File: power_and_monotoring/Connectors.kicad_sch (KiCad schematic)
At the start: 4 parts, among them J2 HLE-108-02-L-DV-BE-K-TR, J3 HLE-108-02-L-DV-BE-K-TR, J4 HLE-108-02-L-DV-BE-K-TR, J5 HLE-108-02-L-DV-BE-K-TR

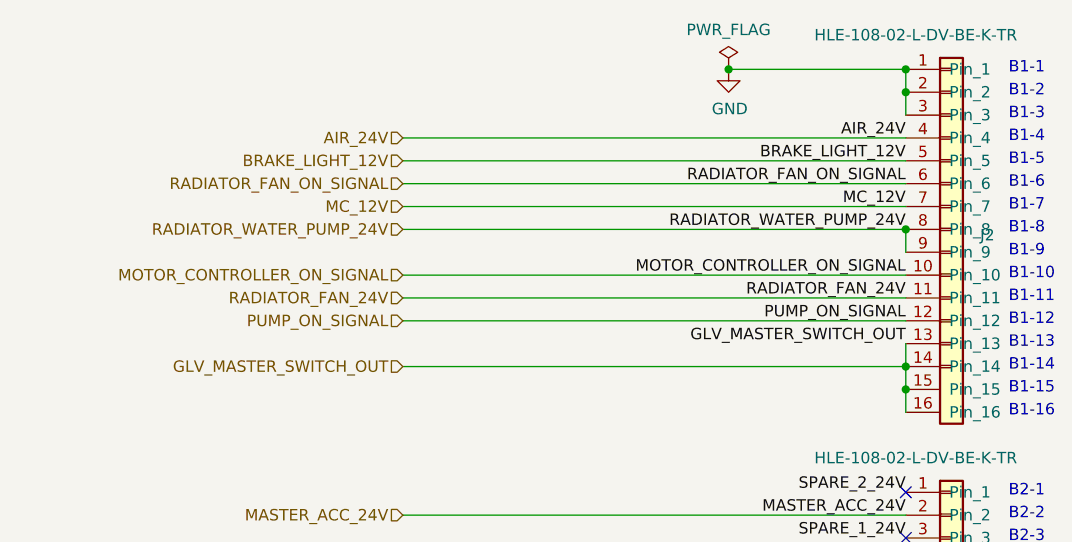
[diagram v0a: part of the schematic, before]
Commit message: first connections done (not perfect yet)
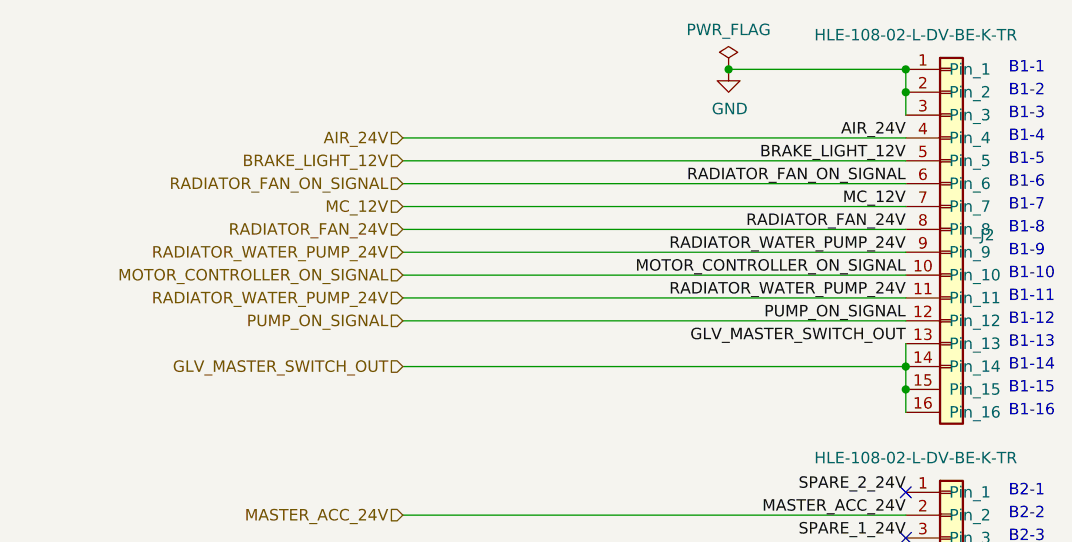
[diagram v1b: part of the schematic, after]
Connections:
- net RADIATOR_FAN_24V: now also J2.8 (Pin_8); no longer J2.11 (Pin_11)
- net RADIATOR_WATER_PUMP_24V: now also J2.11 (Pin_11); no longer J2.8 (Pin_8)
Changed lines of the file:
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@@
   (junction (at 193.675 96.52) (diameter 0) (color 0 0 0 0)
-  )
-  (junction (at 193.675 81.28) (diameter 0) (color 0 0 0 0)
   )
   (junction (at 193.675 63.5) (diameter 0) (color 0 0 0 0)
@@
     (stroke (width 0) (type default))
   )
-  (wire (pts (xy 193.675 81.28) (xy 193.675 83.82))
-    (stroke (width 0) (type default))
-  )
   (wire (pts (xy 137.795 128.27) (xy 193.675 128.27))
     (stroke (width 0) (type default))
   )
+  (wire (pts (xy 137.795 83.82) (xy 193.675 83.82))
+    (stroke (width 0) (type default))
+  )
   (wire (pts (xy 173.99 63.5) (xy 193.675 63.5))
     (stroke (width 0) (type default))
@@
     (stroke (width 0) (type default))
   )
+  (wire (pts (xy 137.795 81.28) (xy 193.675 81.28))
+    (stroke (width 0) (type default))
+  )
   (wire (pts (xy 137.795 73.66) (xy 193.675 73.66))
     (stroke (width 0) (type default))
@@
     (stroke (width 0) (type default))
   )
+  (wire (pts (xy 137.795 140.97) (xy 193.675 140.97))
+    (stroke (width 0) (type default))
+  )
+  (wire (pts (xy 137.795 118.11) (xy 193.675 118.11))
+    (stroke (width 0) (type default))
+  )
   (wire (pts (xy 137.795 88.9) (xy 193.675 88.9))
     (stroke (width 0) (type default))
   )
-  (wire (pts (xy 137.795 140.97) (xy 193.675 140.97))
-    (stroke (width 0) (type default))
-  )
-  (wire (pts (xy 137.795 118.11) (xy 193.675 118.11))
-    (stroke (width 0) (type default))
-  )
   (wire (pts (xy 137.795 86.36) (xy 193.675 86.36))
     (stroke (width 0) (type default))
@@
     (stroke (width 0) (type default))
   )
-  (wire (pts (xy 137.795 81.28) (xy 193.675 81.28))
-    (stroke (width 0) (type default))
-  )
   (wire (pts (xy 137.795 91.44) (xy 193.675 91.44))
     (stroke (width 0) (type default))
@@
     (effects (font (size 1.27 1.27)) (justify right bottom))
   )
+  (label "RADIATOR_WATER_PUMP_24V" (at 193.675 88.9 180) (fields_autoplaced)
+    (effects (font (size 1.27 1.27)) (justify right bottom))
+  )
   (label "MC_OK_INDICATOR" (at 193.675 211.455 180) (fields_autoplaced)
     (effects (font (size 1.27 1.27)) (justify right bottom))
@@
     (effects (font (size 1.27 1.27)) (justify right bottom))
   )
-  (label "RADIATOR_FAN_24V" (at 193.675 88.9 180) (fields_autoplaced)
-    (effects (font (size 1.27 1.27)) (justify right bottom))
-  )
   (label "GLV_MASTER_SWITCH_OUT" (at 193.675 93.98 180) (fields_autoplaced)
     (effects (font (size 1.27 1.27)) (justify right bottom))
@@
     (effects (font (size 1.27 1.27)) (justify right bottom))
   )
+  (label "RADIATOR_WATER_PUMP_24V" (at 193.675 83.82 180) (fields_autoplaced)
+    (effects (font (size 1.27 1.27)) (justify right bottom))
+  )
   (label "MC_12V" (at 193.675 78.74 180) (fields_autoplaced)
     (effects (font (size 1.27 1.27)) (justify right bottom))
@@
     (effects (font (size 1.27 1.27)) (justify right bottom))
   )
-  (label "RADIATOR_WATER_PUMP_24V" (at 193.675 81.28 180) (fields_autoplaced)
-    (effects (font (size 1.27 1.27)) (justify right bottom))
-  )
   (label "SHOULDER_RESET" (at 193.675 184.15 180) (fields_autoplaced)
     (effects (font (size 1.27 1.27)) (justify right bottom))
@@
     (effects (font (size 1.27 1.27)) (justify right bottom))
   )
+  (label "RADIATOR_FAN_24V" (at 193.675 81.28 180) (fields_autoplaced)
+    (effects (font (size 1.27 1.27)) (justify right bottom))
+  )
   (label "DASH_BSPD_LED" (at 193.675 168.91 180) (fields_autoplaced)
     (effects (font (size 1.27 1.27)) (justify right bottom))
@@
     (effects (font (size 1.27 1.27)) (justify right bottom))
   )
+  (hierarchical_label "RADIATOR_WATER_PUMP_24V" (shape input) (at 137.795 83.82 180) (fields_autoplaced)
+    (effects (font (size 1.27 1.27)) (justify right))
+  )
   (hierarchical_label "PRESSURE{slash}TEMP_SENSOR_3_5V" (shape input) (at 137.795 161.29 180) (fields_autoplaced)
     (effects (font (size 1.27 1.27)) (justify right))
@@
     (effects (font (size 1.27 1.27)) (justify right))
   )
+  (hierarchical_label "RADIATOR_FAN_24V" (shape input) (at 137.795 81.28 180) (fields_autoplaced)
+    (effects (font (size 1.27 1.27)) (justify right))
+  )
+  (hierarchical_label "RADIATOR_WATER_PUMP_24V" (shape input) (at 137.795 88.9 180) (fields_autoplaced)
+    (effects (font (size 1.27 1.27)) (justify right))
+  )
   (hierarchical_label "DATALOGGER_24V" (shape input) (at 137.795 135.89 180) (fields_autoplaced)
     (effects (font (size 1.27 1.27)) (justify right))
@@
     (effects (font (size 1.27 1.27)) (justify right))
   )
-  (hierarchical_label "RADIATOR_FAN_24V" (shape input) (at 137.795 88.9 180) (fields_autoplaced)
-    (effects (font (size 1.27 1.27)) (justify right))
-  )
   (hierarchical_label "POWER_SIGNAL" (shape input) (at 137.795 181.61 180) (fields_autoplaced)
     (effects (font (size 1.27 1.27)) (justify right))
@@
     (effects (font (size 1.27 1.27)) (justify right))
   )
-  (hierarchical_label "RADIATOR_WATER_PUMP_24V" (shape input) (at 137.795 81.28 180) (fields_autoplaced)
-    (effects (font (size 1.27 1.27)) (justify right))
-  )

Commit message: Final
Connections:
- no-connect marks 26 -> 28
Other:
- moved on the sheet: J2, J3, J4, J5

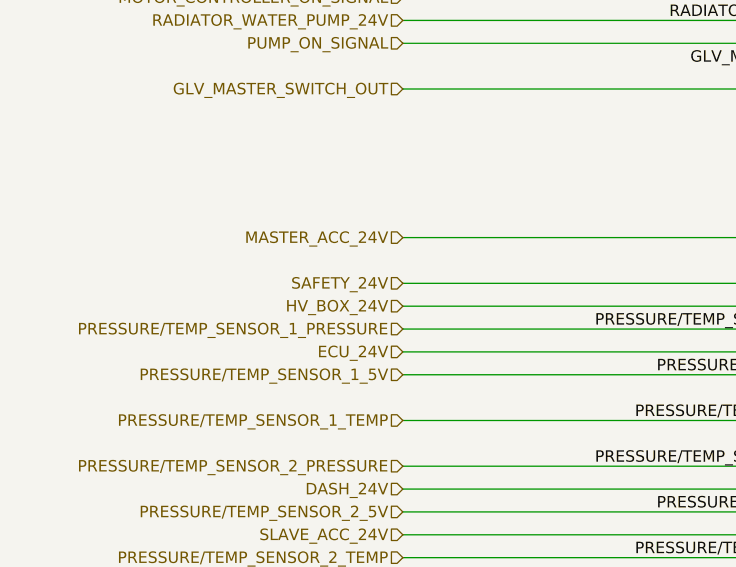
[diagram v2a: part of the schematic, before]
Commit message: Made it 4 layers
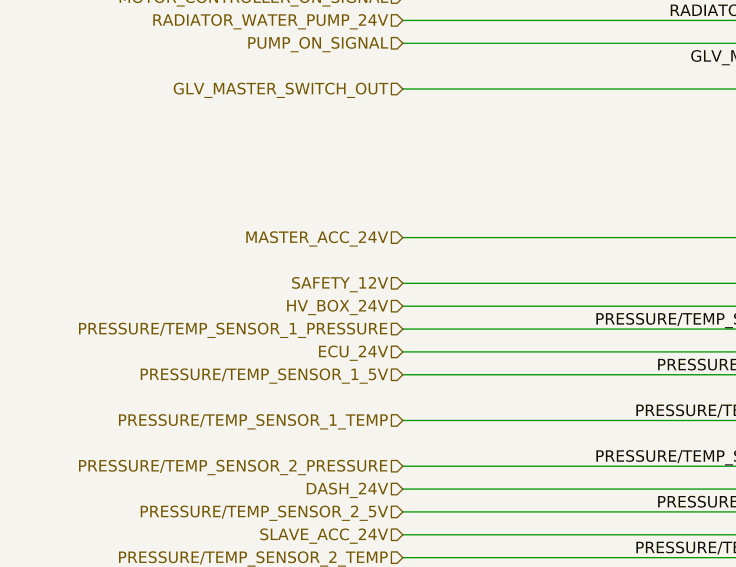
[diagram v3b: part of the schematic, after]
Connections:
- net SAFETY_24V renamed SAFETY_12V
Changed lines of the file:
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@@
 		)
 	)
-	(hierarchical_label "PRESSURE{slash}TEMP_SENSOR_3_TEMP"
+	(hierarchical_label "SAFETY_12V"
 		(shape input)
-		(at 126.238 162.56 180)
+		(at 126.238 114.3 180)
 		(fields_autoplaced yes)
 		(effects
@@
 		)
 	)
-	(hierarchical_label "SAFETY_24V"
+	(hierarchical_label "PRESSURE{slash}TEMP_SENSOR_3_TEMP"
 		(shape input)
-		(at 126.238 114.3 180)
+		(at 126.238 162.56 180)
 		(fields_autoplaced yes)
 		(effects
